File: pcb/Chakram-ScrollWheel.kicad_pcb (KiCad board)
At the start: 2 copper layers, 39.7 x 22.5 mm, 27 parts, among them J1 FPC Connector

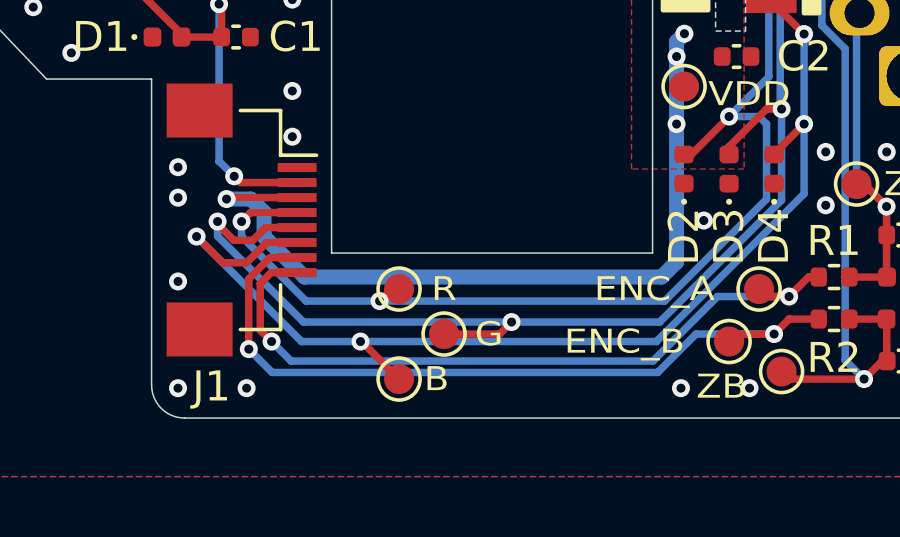
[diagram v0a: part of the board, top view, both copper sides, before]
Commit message: Fixed swapped ENC_A and ENC_B signals on J1
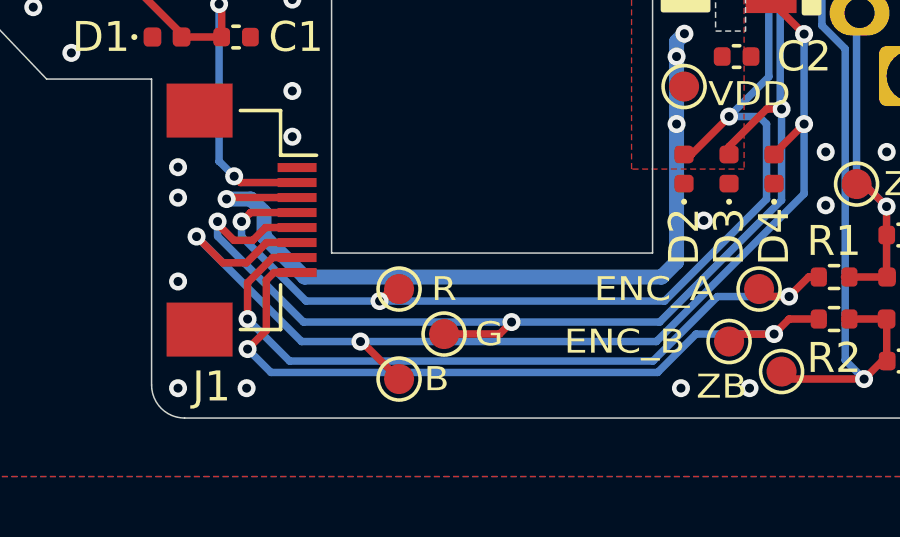
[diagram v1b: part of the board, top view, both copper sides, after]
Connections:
- J1 pad 7: /ENC_B -> /ENC_A
- J1 pad 8: /ENC_A -> /ENC_B
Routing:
- net /ENC_A: track 23.7 -> 24.6 mm
- net /ENC_B: track 25.4 -> 24.9 mm
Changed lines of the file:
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@@
 			(size 0.3 1.3)
 			(layers "F.Cu" "F.Paste" "F.Mask")
-			(net 9 "/ENC_B")
+			(net 10 "/ENC_A")
 			(pinfunction "Pin_7")
 			(pintype "passive")
@@
 			(size 0.3 1.3)
 			(layers "F.Cu" "F.Paste" "F.Mask")
-			(net 10 "/ENC_A")
+			(net 9 "/ENC_B")
 			(pinfunction "Pin_8")
 			(pintype "passive")
@@
 	)
 	(segment
-		(start 65.741051 73.002983)
-		(end 65.741051 70.658949)
-		(width 0.25)
-		(layer "F.Cu")
-		(net 9)
-	)
-	(segment
-		(start 66.45 69.95)
-		(end 67.35 69.95)
+		(start 65.7 73)
+		(end 66.325 72.375)
 		(width 0.25)
 		(layer "F.Cu")
@@
 	)
 	(segment
-		(start 65.741051 70.658949)
-		(end 66.45 69.95)
+		(start 66.325 70.702402)
+		(end 66.577402 70.45)
 		(width 0.25)
 		(layer "F.Cu")
@@
 		(net 9)
 	)
+	(segment
+		(start 66.577402 70.45)
+		(end 67.35 70.45)
+		(width 0.25)
+		(layer "F.Cu")
+		(net 9)
+	)
+	(segment
+		(start 66.325 72.375)
+		(end 66.325 70.702402)
+		(width 0.25)
+		(layer "F.Cu")
+		(net 9)
+	)
 	(via
 		(at 83.25 72.5)
@@
 	)
 	(via
-		(at 65.741051 73.002983)
+		(at 65.7 73)
 		(size 0.6)
 		(drill 0.3)
@@
 	)
 	(segment
-		(start 79.369608 73.78)
-		(end 80.649608 72.5)
+		(start 65.7 73)
+		(end 66.48 73.78)
 		(width 0.25)
 		(layer "B.Cu")
@@
 	)
 	(segment
-		(start 66.518068 73.78)
-		(end 79.369608 73.78)
+		(start 80.649608 72.5)
+		(end 83.25 72.5)
 		(width 0.25)
 		(layer "B.Cu")
@@
 	)
 	(segment
-		(start 65.741051 73.002983)
-		(end 66.518068 73.78)
+		(start 66.48 73.78)
+		(end 79.369608 73.78)
 		(width 0.25)
 		(layer "B.Cu")
@@
 	)
 	(segment
-		(start 80.649608 72.5)
-		(end 83.25 72.5)
+		(start 79.369608 73.78)
+		(end 80.649608 72.5)
 		(width 0.25)
 		(layer "B.Cu")
@@
 	)
 	(segment
-		(start 83.75 71.25)
-		(end 83 71.25)
-		(width 0.25)
-		(layer "F.Cu")
-		(net 10)
-	)
-	(segment
-		(start 84.4 70.6)
-		(end 83.75 71.25)
+		(start 65.7 70.79)
+		(end 66.54 69.95)
 		(width 0.25)
 		(layer "F.Cu")
@@
 	)
 	(segment
-		(start 66.121051 72.371051)
-		(end 66.121051 70.816351)
+		(start 83.75 71.25)
+		(end 83 71.25)
 		(width 0.25)
 		(layer "F.Cu")
@@
 	)
 	(segment
-		(start 66.121051 70.816351)
-		(end 66.487402 70.45)
+		(start 84.4 70.6)
+		(end 83.75 71.25)
 		(width 0.25)
 		(layer "F.Cu")
@@
 	)
 	(segment
-		(start 66.5 72.75)
-		(end 66.121051 72.371051)
+		(start 65.7 72)
+		(end 65.7 70.79)
 		(width 0.25)
 		(layer "F.Cu")
@@
 	)
 	(segment
-		(start 66.487402 70.45)
-		(end 67.35 70.45)
+		(start 66.54 69.95)
+		(end 67.35 69.95)
 		(width 0.25)
 		(layer "F.Cu")
@@
 	)
 	(via
-		(at 66.5 72.75)
+		(at 65.7 72)
 		(size 0.6)
 		(drill 0.3)
@@
 	)
 	(segment
-		(start 67.15 73.4)
-		(end 79.212206 73.4)
+		(start 79.212206 73.4)
+		(end 81.362206 71.25)
 		(width 0.25)
 		(layer "B.Cu")
@@
 	)
 	(segment
-		(start 66.5 72.75)
-		(end 67.15 73.4)
+		(start 67.1 73.4)
+		(end 79.212206 73.4)
 		(width 0.25)
 		(layer "B.Cu")
@@
 	)
 	(segment
-		(start 79.212206 73.4)
-		(end 81.362206 71.25)
+		(start 81.362206 71.25)
+		(end 83.75 71.25)
 		(width 0.25)
 		(layer "B.Cu")
@@
 	)
 	(segment
-		(start 81.362206 71.25)
-		(end 83.75 71.25)
+		(start 65.7 72)
+		(end 67.1 73.4)
 		(width 0.25)
 		(layer "B.Cu")
